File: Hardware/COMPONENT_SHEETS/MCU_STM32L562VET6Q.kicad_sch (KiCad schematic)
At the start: 20 parts, among them IC1 STM32L562VET6Q, J4 I2C1 Debug, J6 UART Debug, J7 SPI 1 Debug, Y1 32MHz

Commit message: Added 3D models to components
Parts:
- Y1: footprint Crystal:Crystal_HC49-4H_Vertical -> RDT_Custom_Footprints:XTAL_ABM7-32.000MHZ-D2Y-T
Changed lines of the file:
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@@
     (property "Reference" "Y1" (id 0) (at 129.54 90.17 0))
     (property "Value" "32MHz" (id 1) (at 127 90.17 0))
-    (property "Footprint" "Crystal:Crystal_HC49-4H_Vertical" (id 2) (at 121.92 90.17 0)
+    (property "Footprint" "RDT_Custom_Footprints:XTAL_ABM7-32.000MHZ-D2Y-T" (id 2) (at 121.92 90.17 0)
       (effects (font (size 1.27 1.27)) hide)
     )

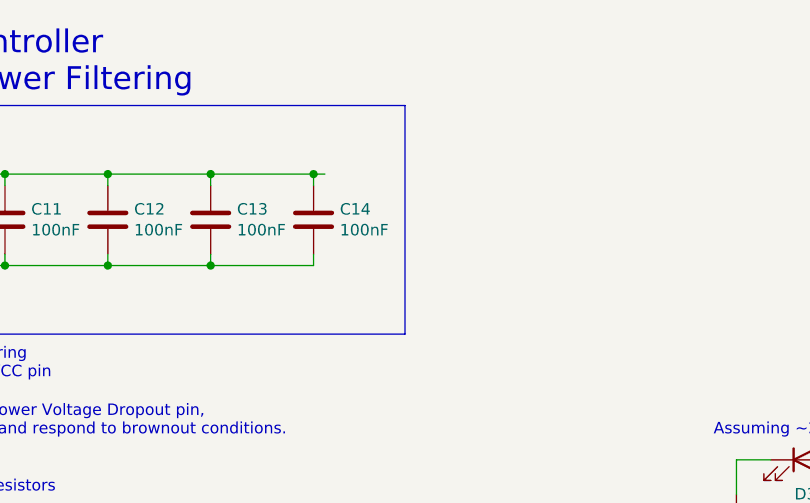
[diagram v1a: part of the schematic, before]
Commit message: Updated MCU Component Sheet
Used the file from the Telemetry board for compatibility and commonality.
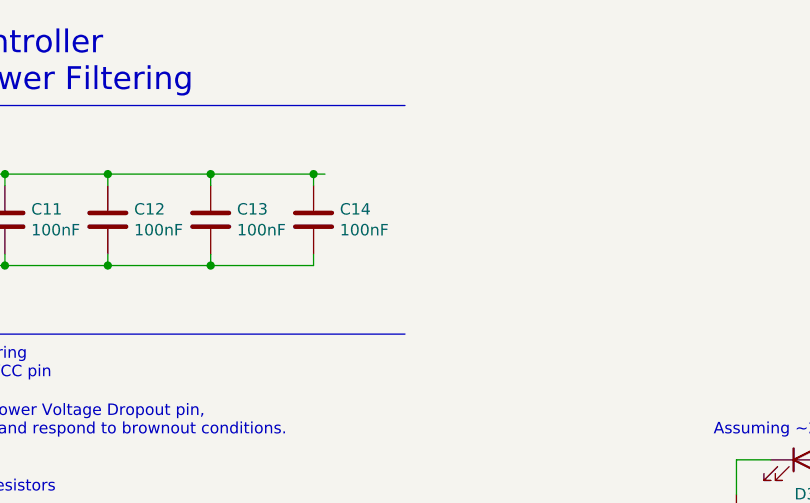
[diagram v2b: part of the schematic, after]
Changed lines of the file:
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@@
-    (stroke (width 0) (type default) (color 0 0 0 0))
-  )
-  (polyline (pts (xy 77.47 49.53) (xy 77.47 24.13))
     (stroke (width 0) (type default) (color 0 0 0 0))
   )
